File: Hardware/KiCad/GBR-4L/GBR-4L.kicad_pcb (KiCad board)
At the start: 4 copper layers, 160 x 100 mm, 188 parts, among them J1 USB4105-GF-A, J101 EM7565 M.2 Key B socket, J102 MODEM_CONTROL, J201 EM7565 M.2 Key B socket, J202 MODEM_CONTROL, J301 EM7565 M.2 Key B socket, J302 MODEM_CONTROL, J401 EM7565 M.2 Key B socket, J402 MODEM_CONTROL, J511 2452808-1 nano-SIM, J521 2452808-1 nano-SIM, J531 2452808-1 nano-SIM, J541 2452808-1 nano-SIM, J701 12V INPUT 5A, Q701 30V P-MOSFET low-RDS(on), Q911 MMBT3906, Q921 MMBT3906, Q931 MMBT3906, Q941 MMBT3906, SW911 MODEM 1 RESET, SW912 MODEM 1 RF DISABLE, SW921 MODEM 2 RESET, SW922 MODEM 2 RF DISABLE, SW931 MODEM 3 RESET, SW932 MODEM 3 RF DISABLE, SW941 MODEM 4 RESET, SW942 MODEM 4 RF DISABLE, U1 USBLC6-2SC6, U11 LOW-CAP SIM ESD ARRAY, U12 LOW-CAP SIM ESD ARRAY, U13 LOW-CAP SIM ESD ARRAY, U14 LOW-CAP SIM ESD ARRAY, U2 USB2514Bi-I/M2, U21 TPS56339DDCR, U22 TPS56339DDCR, U23 TPS56339DDCR, U24 TPS56339DDCR, U25 TPS56339DDCR, Y1 24MHz

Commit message: Place USB hub and thermal vias
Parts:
- moved U2 99.1 mm to (145.0, 55.0)
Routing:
- net GND: vias 51 -> 55
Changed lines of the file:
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@@
 	(footprint "Package_DFN_QFN:QFN-36-1EP_6x6mm_P0.5mm_EP4.1x4.1mm"
 		(layer "F.Cu")
-		(at 47.53 37.155001)
+		(at 145 55)
 		(descr "QFN, 36 Pin (www.st.com/resource/en/datasheet/stm32f101t6.pdf#page=72)")
 		(tags "QFN NoLead")
@@
 	)
 	(via
+		(at 144.2 55.8)
+		(size 0.6)
+		(drill 0.3)
+		(layers "F.Cu" "B.Cu")
+		(tenting
+			(front no)
+			(back yes)
+		)
+		(net "GND")
+	)
+	(via
 		(at 125 75)
 		(size 0.6)
@@
 	)
 	(via
+		(at 145.8 55.8)
+		(size 0.6)
+		(drill 0.3)
+		(layers "F.Cu" "B.Cu")
+		(tenting
+			(front no)
+			(back yes)
+		)
+		(net "GND")
+	)
+	(via
 		(at 110 117)
 		(size 0.6)
@@
 		(net "GND")
 	)
+	(via
+		(at 144.2 54.2)
+		(size 0.6)
+		(drill 0.3)
+		(layers "F.Cu" "B.Cu")
+		(tenting
+			(front no)
+			(back yes)
+		)
+		(net "GND")
+	)
+	(via
+		(at 145.8 54.2)
+		(size 0.6)
+		(drill 0.3)
+		(layers "F.Cu" "B.Cu")
+		(tenting
+			(front no)
+			(back yes)
+		)
+		(net "GND")
+	)

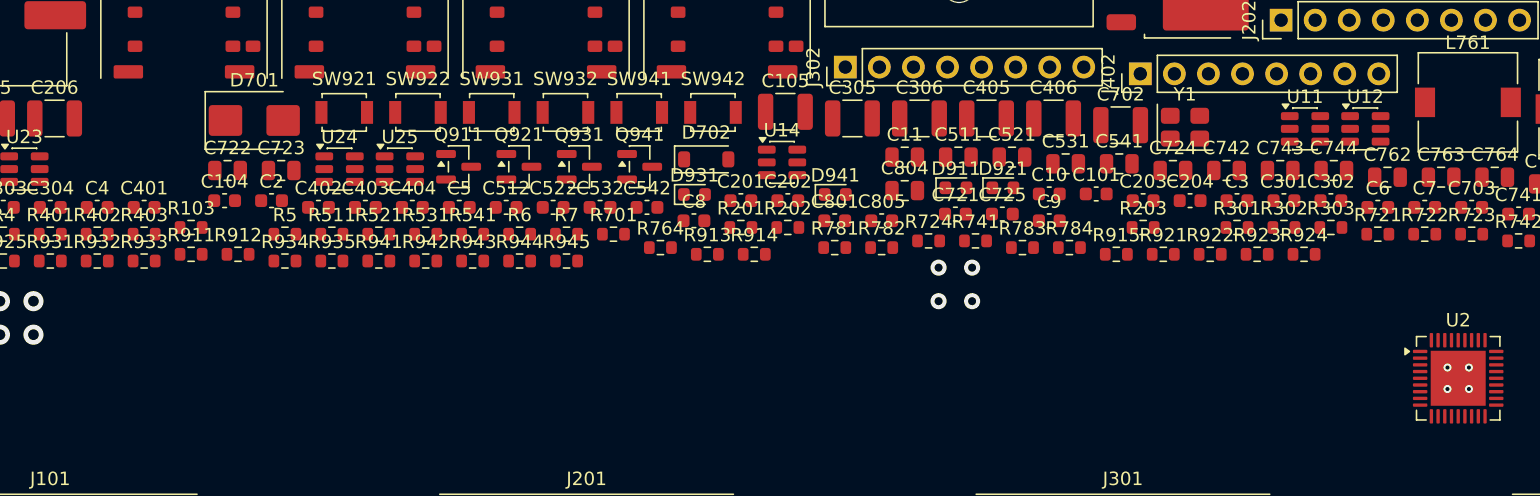
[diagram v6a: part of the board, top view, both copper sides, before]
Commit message: Place and route USB hub oscillator
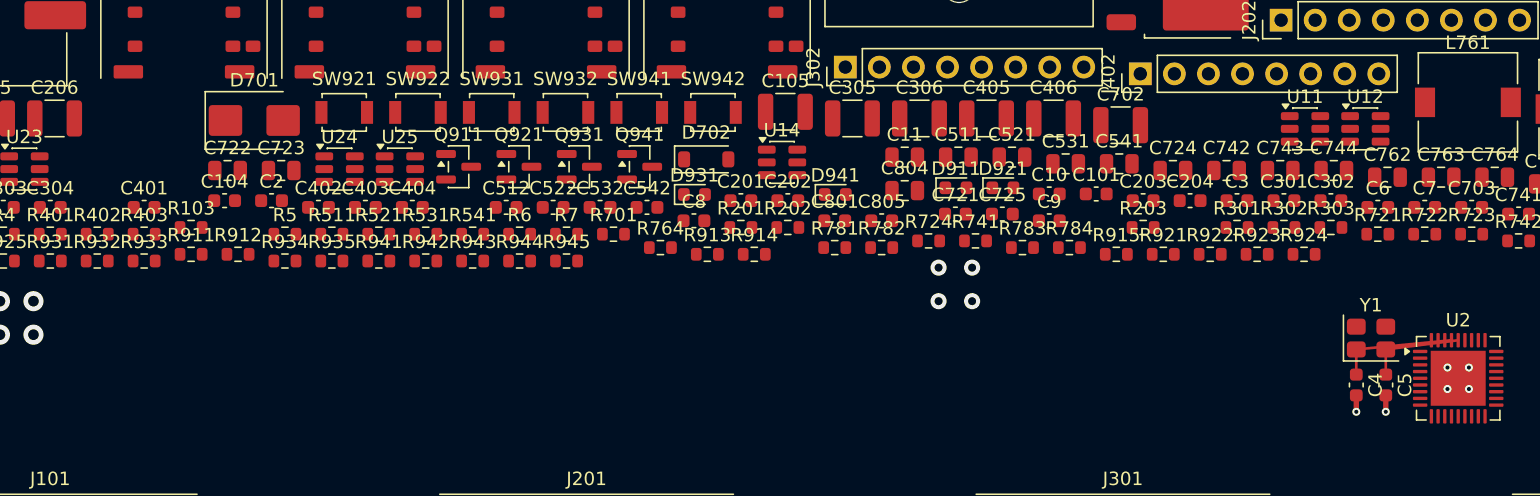
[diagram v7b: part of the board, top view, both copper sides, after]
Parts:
- moved C4 94.8 mm to (137.4, 55.5), turned to -90 degrees
- moved C5 70.4 mm to (139.6, 55.5), turned to -90 degrees
- moved Y1 21.0 mm to (138.5, 52.0)
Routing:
- net HUB_XTALIN: track 0.00 -> 9.01 mm
- net HUB_XTALOUT: track 0.00 -> 7.32 mm
- net GND: track 15.5 -> 18.0 mm, vias 55 -> 57
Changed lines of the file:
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@@
 	(footprint "Capacitor_SMD:C_0603_1608Metric"
 		(layer "F.Cu")
-		(at 70.505001 42.254999)
+		(at 139.6 55.5 -90)
 		(descr "Capacitor SMD 0603 (1608 Metric), square (rectangular) end terminal, IPC-7351 nominal, (Body size source: IPC-SM-782 page 76, https://www.pcb-3d.com/wordpress/wp-content/uploads/ipc-sm-782a_amendment_1_and_2.pdf)")
 		(tags "capacitor")
 		(property "Reference" "C5"
-			(at 0 -1.43 0)
+			(at 0 -1.43 270)
 			(layer "F.SilkS")
 			(effects
@@
 		)
 		(property "Value" "12pF C0G"
-			(at 0 1.43 0)
+			(at 0 1.43 270)
 			(layer "F.Fab")
 			(effects
@@
 		)
 		(property "Datasheet" ""
-			(at 0 0 0)
+			(at 0 0 270)
 			(layer "F.Fab")
 			(hide yes)
@@
 		)
 		(property "Description" ""
-			(at 0 0 0)
+			(at 0 0 270)
 			(layer "F.Fab")
 			(hide yes)
@@
 		)
 		(property "KiLib_Generator" "SMD_2terminal_chip_molded"
-			(at 0 0 0)
+			(at 0 0 270)
 			(layer "F.SilkS")
 			(hide yes)
@@
 		(duplicate_pad_numbers_are_jumpers no)
 		(fp_line
-			(start -0.14058 -0.51)
-			(end 0.14058 -0.51)
+			(start -0.14058 0.51)
+			(end 0.14058 0.51)
 			(stroke
 				(width 0.12)
@@
 		)
 		(fp_line
-			(start -0.14058 0.51)
-			(end 0.14058 0.51)
+			(start -0.14058 -0.51)
+			(end 0.14058 -0.51)
 			(stroke
 				(width 0.12)
@@
 		)
 		(fp_text user "${REFERENCE}"
-			(at 0 0 0)
+			(at 0 0 270)
 			(layer "F.Fab")
 			(effects
@@
 		)
 		(pad "1" smd roundrect
-			(at -0.775 0)
+			(at -0.775 0 270)
 			(size 0.9 0.95)
 			(layers "F.Cu" "F.Mask" "F.Paste")
@@
 		)
 		(pad "2" smd roundrect
-			(at 0.775 0)
+			(at 0.775 0 270)
 			(size 0.9 0.95)
 			(layers "F.Cu" "F.Mask" "F.Paste")
@@
 	(footprint "Capacitor_SMD:C_0603_1608Metric"
 		(layer "F.Cu")
-		(at 43.505 42.255)
+		(at 137.4 55.5 -90)
 		(descr "Capacitor SMD 0603 (1608 Metric), square (rectangular) end terminal, IPC-7351 nominal, (Body size source: IPC-SM-782 page 76, https://www.pcb-3d.com/wordpress/wp-content/uploads/ipc-sm-782a_amendment_1_and_2.pdf)")
 		(tags "capacitor")
 		(property "Reference" "C4"
-			(at 0 -1.43 0)
+			(at 0 -1.43 270)
 			(layer "F.SilkS")
 			(effects
@@
 		)
 		(property "Value" "12pF C0G"
-			(at 0 1.43 0)
+			(at 0 1.43 270)
 			(layer "F.Fab")
 			(effects
@@
 		)
 		(property "Datasheet" ""
-			(at 0 0 0)
+			(at 0 0 270)
 			(layer "F.Fab")
 			(hide yes)
@@
 		)
 		(property "Description" ""
-			(at 0 0 0)
+			(at 0 0 270)
 			(layer "F.Fab")
 			(hide yes)
@@
 		)
 		(property "KiLib_Generator" "SMD_2terminal_chip_molded"
-			(at 0 0 0)
+			(at 0 0 270)
 			(layer "F.SilkS")
 			(hide yes)
@@
 		(duplicate_pad_numbers_are_jumpers no)
 		(fp_line
-			(start -0.14058 -0.51)
-			(end 0.14058 -0.51)
+			(start -0.14058 0.51)
+			(end 0.14058 0.51)
 			(stroke
 				(width 0.12)
@@
 		)
 		(fp_line
-			(start -0.14058 0.51)
-			(end 0.14058 0.51)
+			(start -0.14058 -0.51)
+			(end 0.14058 -0.51)
 			(stroke
 				(width 0.12)
@@
 		)
 		(fp_text user "${REFERENCE}"
-			(at 0 0 0)
+			(at 0 0 270)
 			(layer "F.Fab")
 			(effects
@@
 		)
 		(pad "1" smd roundrect
-			(at -0.775 0)
+			(at -0.775 0 270)
 			(size 0.9 0.95)
 			(layers "F.Cu" "F.Mask" "F.Paste")
@@
 		)
 		(pad "2" smd roundrect
-			(at 0.775 0)
+			(at 0.775 0 270)
 			(size 0.9 0.95)
 			(layers "F.Cu" "F.Mask" "F.Paste")
@@
 	(footprint "Crystal:Crystal_SMD_3225-4Pin_3.2x2.5mm"
 		(layer "F.Cu")
-		(at 124.625 36.275001)
+		(at 138.5 52)
 		(descr "SMD3225/4, Crystal, 3.2x2.5mm package, SMD, http://www.txccrystal.com/images/pdf/7m-accuracy.pdf")
 		(property "Reference" "Y1"
@@
 	)
 	(segment
+		(start 137.4 56.275)
+		(end 137.4 57.5)
+		(width 0.4)
+		(layer "F.Cu")
+		(net "GND")
+	)
+	(segment
 		(start 170.325 54)
 		(end 170.325 56)
@@
 	)
 	(segment
+		(start 139.6 56.275)
+		(end 139.6 57.5)
+		(width 0.4)
+		(layer "F.Cu")
+		(net "GND")
+	)
+	(segment
 		(start 171.32 31.8)
 		(end 168.5 31.8)
@@
 	)
 	(via
+		(at 137.4 57.5)
+		(size 0.6)
+		(drill 0.3)
+		(layers "F.Cu" "B.Cu")
+		(net "GND")
+	)
+	(via
 		(at 75 75)
 		(size 0.6)
@@
 	)
 	(via
+		(at 139.6 57.5)
+		(size 0.6)
+		(drill 0.3)
+		(layers "F.Cu" "B.Cu")
+		(net "GND")
+	)
+	(via
 		(at 125 75)
 		(size 0.6)
@@
 	)
 	(segment
+		(start 139.6 52.85)
+		(end 145 52.1625)
+		(width 0.2)
+		(layer "F.Cu")
+		(net "HUB_XTALOUT")
+	)
+	(segment
+		(start 139.6 52.85)
+		(end 139.6 54.725)
+		(width 0.2)
+		(layer "F.Cu")
+		(net "HUB_XTALOUT")
+	)
+	(segment
 		(start 171.9 39.32)
 		(end 168.5 39.32)
@@
 		(net "USB_SHIELD")
 	)
+	(segment
+		(start 137.4 52.85)
+		(end 137.4 54.725)
+		(width 0.2)
+		(layer "F.Cu")
+		(net "HUB_XTALIN")
+	)
+	(segment
+		(start 137.4 52.85)
+		(end 144.5 52.1625)
+		(width 0.2)
+		(layer "F.Cu")
+		(net "HUB_XTALIN")
+	)
 	(zone
